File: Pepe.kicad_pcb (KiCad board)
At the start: 2 copper layers, 10 parts, among them P1 USB_OTG, P2 VOC_CONN, P3 DBG_SETPOINT, P4 DBG_VOC, P5 DBG_OUTPUT, U1 ADCMP371, U2 APT7335A-50

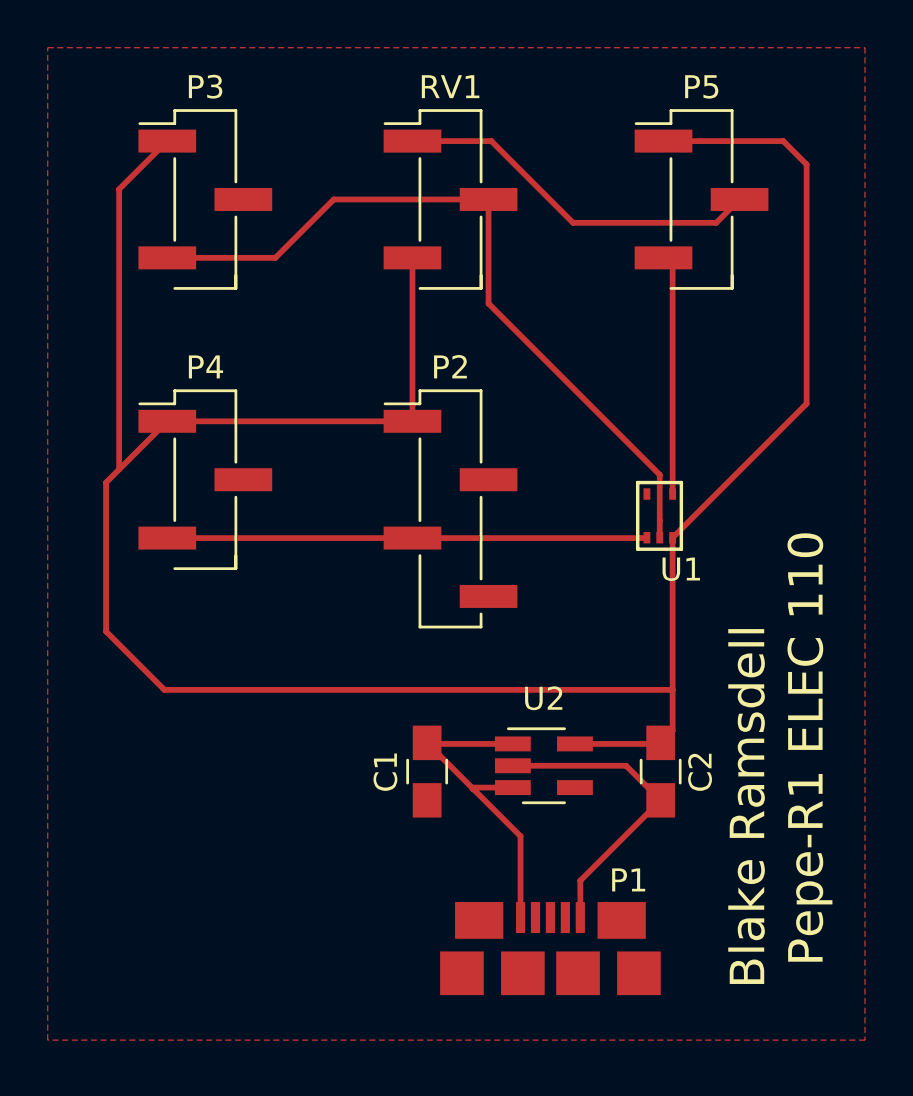
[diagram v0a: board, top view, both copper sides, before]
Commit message: Redid PCB with new comparator. Needs more ground plane work.
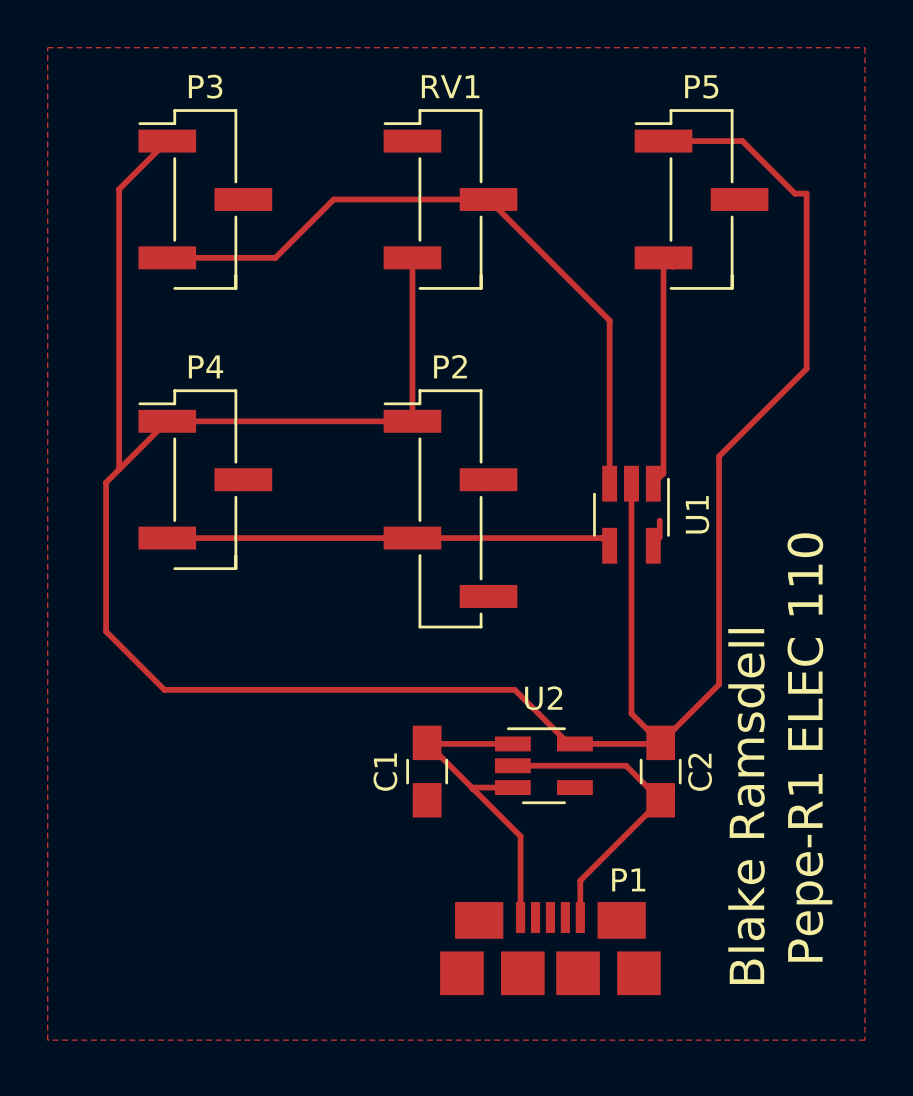
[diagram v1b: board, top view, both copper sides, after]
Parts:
- U1: value ADCMP371 -> MIC7211YM5; footprint Pepe:SC70 -> TO_SOT_Packages_SMD:SOT-23-5_HandSoldering
- moved U1 1.27 mm to (91.4, 61.0), turned to 270 degrees
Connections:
- U1 pad 1: VOC -> OUTPUT
- U1 pad 2: SETPOINT -> +5V
- U1 pad 3: +5V -> SETPOINT
- U1 pad 4: GND -> VOC
- U1 pad 5: OUTPUT -> GND
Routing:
- net GND: track 29.7 -> 14.3 mm
- net +5V: track 107.1 -> 115.6 mm
- net SETPOINT: track 32.8 -> 29.6 mm
- net VOC: track 20.9 -> 19.4 mm
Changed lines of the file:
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@@
     (thickness 1.6)
     (drawings 2)
-    (tracks 46)
+    (tracks 47)
     (zones 0)
     (modules 10)
@@
     (add_net ~ENABLE)
   )
+  (module TO_SOT_Packages_SMD:SOT-23-5_HandSoldering (layer F.Cu)
+    (at 91.44 60.96 270)
+    (descr "5-pin SOT23 package")
+    (tags "SOT-23-5 hand-soldering")
+    (attr smd)
+    (fp_text reference U1 (at 0 -2.9 270) (layer F.SilkS)
+      (effects (font (size 1 1) (thickness 0.15)))
+    )
+    (fp_text value MIC7211YM5 (at 0 2.9 270) (layer F.Fab) hide
+      (effects (font (size 1 1) (thickness 0.15)))
+    )
+    (fp_text user %R (at 0 0) (layer F.Fab)
+      (effects (font (size 0.5 0.5) (thickness 0.075)))
+    )
+    (fp_line (start -0.9 1.61) (end 0.9 1.61) (layer F.SilkS) (width 0.12))
+    (fp_line (start 0.9 -1.61) (end -1.55 -1.61) (layer F.SilkS) (width 0.12))
+    (fp_line (start -0.9 -0.9) (end -0.25 -1.55) (layer F.Fab) (width 0.1))
+    (fp_line (start 0.9 -1.55) (end -0.25 -1.55) (layer F.Fab) (width 0.1))
+    (fp_line (start -0.9 -0.9) (end -0.9 1.55) (layer F.Fab) (width 0.1))
+    (fp_line (start 0.9 1.55) (end -0.9 1.55) (layer F.Fab) (width 0.1))
+    (fp_line (start 0.9 -1.55) (end 0.9 1.55) (layer F.Fab) (width 0.1))
+    (fp_line (start -2.38 -1.8) (end 2.38 -1.8) (layer F.CrtYd) (width 0.05))
+    (fp_line (start -2.38 -1.8) (end -2.38 1.8) (layer F.CrtYd) (width 0.05))
+    (fp_line (start 2.38 1.8) (end 2.38 -1.8) (layer F.CrtYd) (width 0.05))
+    (fp_line (start 2.38 1.8) (end -2.38 1.8) (layer F.CrtYd) (width 0.05))
+    (pad 1 smd rect (at -1.35 -0.95 270) (size 1.56 0.65) (layers F.Cu F.Paste F.Mask)
+      (net 11 OUTPUT))
+    (pad 2 smd rect (at -1.35 0 270) (size 1.56 0.65) (layers F.Cu F.Paste F.Mask)
+      (net 3 +5V))
+    (pad 3 smd rect (at -1.35 0.95 270) (size 1.56 0.65) (layers F.Cu F.Paste F.Mask)
+      (net 10 SETPOINT))
+    (pad 4 smd rect (at 1.35 0.95 270) (size 1.56 0.65) (layers F.Cu F.Paste F.Mask)
+      (net 9 VOC))
+    (pad 5 smd rect (at 1.35 -0.95 270) (size 1.56 0.65) (layers F.Cu F.Paste F.Mask)
+      (net 1 GND))
+    (model ${KISYS3DMOD}/TO_SOT_Packages_SMD.3dshapes\SOT-23-5.wrl
+      (at (xyz 0 0 0))
+      (scale (xyz 1 1 1))
+      (rotate (xyz 0 0 0))
+    )
+  )
   (module Capacitors_SMD:C_0805_HandSoldering (layer F.Cu)
     (at 82.55 72.136 270)
@@
     )
   )
-  (module Pepe:SC70 (layer F.Cu)
-    (at 92.71 60.96)
-    (fp_text reference U1 (at 0.9 2.4) (layer F.SilkS)
-      (effects (font (size 1 1) (thickness 0.15)))
-    )
-    (fp_text value ADCMP371 (at 0.7 -2.2) (layer F.Fab) hide
-      (effects (font (size 1 1) (thickness 0.15)))
-    )
-    (fp_line (start -1 1.5) (end -1 -1.4) (layer F.SilkS) (width 0.15))
-    (fp_line (start 0.9 1.5) (end -1 1.5) (layer F.SilkS) (width 0.15))
-    (fp_line (start 0.9 -1.4) (end 0.9 1.5) (layer F.SilkS) (width 0.15))
-    (fp_line (start -1 -1.4) (end 0.9 -1.4) (layer F.SilkS) (width 0.15))
-    (pad 5 smd rect (at 0.52 -0.9) (size 0.3 0.5) (layers F.Cu F.Paste F.Mask)
-      (net 11 OUTPUT))
-    (pad 4 smd rect (at -0.6 -0.9) (size 0.3 0.5) (layers F.Cu F.Paste F.Mask)
-      (net 1 GND))
-    (pad 3 smd rect (at 0.52 1) (size 0.3 0.5) (layers F.Cu F.Paste F.Mask)
-      (net 3 +5V))
-    (pad 2 smd rect (at -0.04 1) (size 0.3 0.5) (layers F.Cu F.Paste F.Mask)
-      (net 10 SETPOINT))
-    (pad 1 smd rect (at -0.6 1) (size 0.3 0.5) (layers F.Cu F.Paste F.Mask)
-      (net 9 VOC))
-  )
   (module TO_SOT_Packages_SMD:SOT-23-5_HandSoldering (layer F.Cu)
     (at 87.63 71.882)
@@
     (effects (font (size 1.5 1.5) (thickness 0.3)))
   )
-  (segment (start 81.911 44.704) (end 85.344 44.704) (width 0.25) (layer F.Cu) (net 1) (status 400000))
-  (segment (start 95.127 48.26) (end 96.143 47.244) (width 0.25) (layer F.Cu) (net 1) (status 800000))
-  (segment (start 88.9 48.26) (end 95.127 48.26) (width 0.25) (layer F.Cu) (net 1))
-  (segment (start 85.344 44.704) (end 88.9 48.26) (width 0.25) (layer F.Cu) (net 1))
   (segment (start 86.28 71.882) (end 91.206 71.882) (width 0.25) (layer F.Cu) (net 1) (status 400000))
   (segment (start 91.206 71.882) (end 92.71 73.386) (width 0.25) (layer F.Cu) (net 1) (status 800000))
@@
   (segment (start 84.582 72.918) (end 86.614 74.95) (width 0.25) (layer F.Cu) (net 2))
   (segment (start 86.614 74.95) (end 86.614 78.486) (width 0.25) (layer F.Cu) (net 2) (status 800000))
+  (segment (start 99.06 46.99) (end 99.06 54.61) (width 0.25) (layer F.Cu) (net 3))
+  (segment (start 96.266 44.704) (end 98.552 46.99) (width 0.25) (layer F.Cu) (net 3))
+  (segment (start 98.552 46.99) (end 99.06 46.99) (width 0.25) (layer F.Cu) (net 3))
+  (segment (start 92.833 44.704) (end 96.266 44.704) (width 0.25) (layer F.Cu) (net 3) (status 400000))
+  (segment (start 95.25 68.346) (end 92.71 70.886) (width 0.25) (layer F.Cu) (net 3) (status 800000))
+  (segment (start 95.25 58.42) (end 95.25 68.346) (width 0.25) (layer F.Cu) (net 3))
+  (segment (start 99.06 54.61) (end 95.25 58.42) (width 0.25) (layer F.Cu) (net 3))
+  (segment (start 91.44 59.61) (end 91.44 69.616) (width 0.25) (layer F.Cu) (net 3) (status 400000))
+  (segment (start 91.44 69.616) (end 92.71 70.886) (width 0.25) (layer F.Cu) (net 3) (status 800000))
+  (segment (start 88.98 70.932) (end 88.712 70.932) (width 0.25) (layer F.Cu) (net 3) (status C00000))
+  (segment (start 88.712 70.932) (end 86.36 68.58) (width 0.25) (layer F.Cu) (net 3) (status 400000))
   (segment (start 69.1495 58.9895) (end 69.1495 46.7975) (width 0.25) (layer F.Cu) (net 3))
   (segment (start 69.1495 46.7975) (end 71.243 44.704) (width 0.25) (layer F.Cu) (net 3) (status 800000))
   (segment (start 71.243 56.896) (end 81.911 56.896) (width 0.25) (layer F.Cu) (net 3) (status C00000))
-  (segment (start 93.23 68.58) (end 71.12 68.58) (width 0.25) (layer F.Cu) (net 3))
+  (segment (start 86.36 68.58) (end 71.12 68.58) (width 0.25) (layer F.Cu) (net 3))
   (segment (start 68.58 59.559) (end 69.1495 58.9895) (width 0.25) (layer F.Cu) (net 3))
   (segment (start 69.1495 58.9895) (end 71.243 56.896) (width 0.25) (layer F.Cu) (net 3) (status 800000))
   (segment (start 68.58 66.04) (end 68.58 59.559) (width 0.25) (layer F.Cu) (net 3))
   (segment (start 71.12 68.58) (end 68.58 66.04) (width 0.25) (layer F.Cu) (net 3))
-  (segment (start 92.833 44.704) (end 98.044 44.704) (width 0.25) (layer F.Cu) (net 3) (status 400000))
-  (segment (start 99.06 56.13) (end 93.23 61.96) (width 0.25) (layer F.Cu) (net 3) (status 800000))
-  (segment (start 99.06 45.72) (end 99.06 56.13) (width 0.25) (layer F.Cu) (net 3))
-  (segment (start 98.044 44.704) (end 99.06 45.72) (width 0.25) (layer F.Cu) (net 3))
   (segment (start 81.911 49.784) (end 81.911 56.896) (width 0.25) (layer F.Cu) (net 3) (status C00000))
-  (segment (start 93.23 61.96) (end 93.23 68.58) (width 0.25) (layer F.Cu) (net 3) (status 400000))
-  (segment (start 93.23 68.58) (end 93.23 70.366) (width 0.25) (layer F.Cu) (net 3) (status 800000))
   (segment (start 93.23 70.366) (end 92.71 70.886) (width 0.25) (layer F.Cu) (net 3) (status C00000))
   (segment (start 88.98 70.932) (end 92.664 70.932) (width 0.25) (layer F.Cu) (net 3) (status C00000))
   (segment (start 92.664 70.932) (end 92.71 70.886) (width 0.25) (layer F.Cu) (net 3) (status C00000))
+  (segment (start 81.911 61.976) (end 90.156 61.976) (width 0.25) (layer F.Cu) (net 9) (status 400000))
+  (segment (start 90.156 61.976) (end 90.49 62.31) (width 0.25) (layer F.Cu) (net 9) (status 800000))
   (segment (start 71.243 61.976) (end 81.911 61.976) (width 0.25) (layer F.Cu) (net 9) (status C00000))
-  (segment (start 81.911 61.976) (end 92.094 61.976) (width 0.25) (layer F.Cu) (net 9) (status C00000))
-  (segment (start 92.094 61.976) (end 92.11 61.96) (width 0.25) (layer F.Cu) (net 9) (status C00000))
+  (segment (start 90.49 59.61) (end 90.49 52.513) (width 0.25) (layer F.Cu) (net 10) (status 400000))
+  (segment (start 90.49 52.513) (end 85.221 47.244) (width 0.25) (layer F.Cu) (net 10) (status 800000))
   (segment (start 71.243 49.784) (end 75.946 49.784) (width 0.25) (layer F.Cu) (net 10) (status 400000))
   (segment (start 78.486 47.244) (end 85.221 47.244) (width 0.25) (layer F.Cu) (net 10) (status 800000))
   (segment (start 75.946 49.784) (end 78.486 47.244) (width 0.25) (layer F.Cu) (net 10))
-  (segment (start 92.67 61.96) (end 92.67 61.214) (width 0.25) (layer F.Cu) (net 10) (status 400000))
-  (segment (start 92.67 61.214) (end 92.67 59.222) (width 0.25) (layer F.Cu) (net 10))
-  (segment (start 85.221 51.773) (end 85.221 47.244) (width 0.25) (layer F.Cu) (net 10) (status 800000))
-  (segment (start 92.67 59.222) (end 85.221 51.773) (width 0.25) (layer F.Cu) (net 10))
-  (segment (start 93.23 60.06) (end 93.23 50.181) (width 0.25) (layer F.Cu) (net 11) (status C00000))
+  (segment (start 92.67 61.96) (end 92.67 61.214) (width 0.25) (layer F.Cu) (net 1) (status 400000))
+  (segment (start 92.833 49.784) (end 92.833 59.167) (width 0.25) (layer F.Cu) (net 11) (status 400000))
+  (segment (start 92.833 59.167) (end 92.39 59.61) (width 0.25) (layer F.Cu) (net 11) (status 800000))
   (segment (start 93.23 50.181) (end 92.833 49.784) (width 0.25) (layer F.Cu) (net 11) (status C00000))
   (zone (net 1) (net_name GND) (layer F.Cu) (hatch edge 0.508)

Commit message: R1 PCB might be done. No ERC or DRC errors.
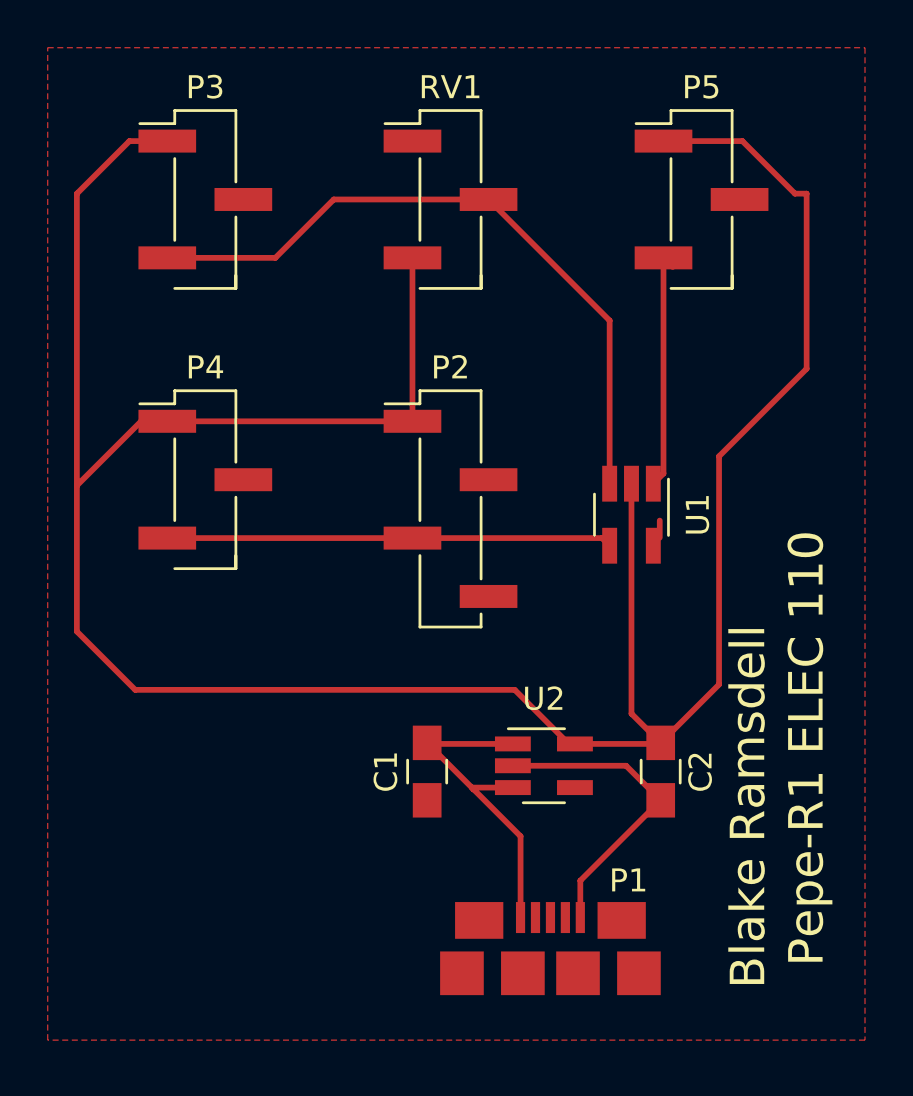
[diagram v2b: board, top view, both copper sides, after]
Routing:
- net +5V: track 115.6 -> 120.5 mm
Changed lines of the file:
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@@
     (thickness 1.6)
     (drawings 2)
-    (tracks 47)
+    (tracks 48)
     (zones 0)
     (modules 10)
@@
   (segment (start 84.582 72.918) (end 86.614 74.95) (width 0.25) (layer F.Cu) (net 2))
   (segment (start 86.614 74.95) (end 86.614 78.486) (width 0.25) (layer F.Cu) (net 2) (status 800000))
+  (segment (start 67.31 59.69) (end 67.31 46.99) (width 0.25) (layer F.Cu) (net 3))
+  (segment (start 69.596 44.704) (end 71.243 44.704) (width 0.25) (layer F.Cu) (net 3) (status 800000))
+  (segment (start 67.31 46.99) (end 69.596 44.704) (width 0.25) (layer F.Cu) (net 3))
+  (segment (start 67.31 66.04) (end 67.31 59.69) (width 0.25) (layer F.Cu) (net 3))
+  (segment (start 86.36 68.58) (end 69.85 68.58) (width 0.25) (layer F.Cu) (net 3))
+  (segment (start 69.85 68.58) (end 67.31 66.04) (width 0.25) (layer F.Cu) (net 3))
+  (segment (start 88.712 70.932) (end 86.36 68.58) (width 0.25) (layer F.Cu) (net 3) (status 400000))
+  (segment (start 67.31 59.69) (end 70.104 56.896) (width 0.25) (layer F.Cu) (net 3) (status 800000))
+  (segment (start 70.104 56.896) (end 71.243 56.896) (width 0.25) (layer F.Cu) (net 3) (status C00000))
+  (segment (start 88.98 70.932) (end 88.712 70.932) (width 0.25) (layer F.Cu) (net 3) (status C00000))
   (segment (start 99.06 46.99) (end 99.06 54.61) (width 0.25) (layer F.Cu) (net 3))
   (segment (start 96.266 44.704) (end 98.552 46.99) (width 0.25) (layer F.Cu) (net 3))
@@
   (segment (start 91.44 59.61) (end 91.44 69.616) (width 0.25) (layer F.Cu) (net 3) (status 400000))
   (segment (start 91.44 69.616) (end 92.71 70.886) (width 0.25) (layer F.Cu) (net 3) (status 800000))
-  (segment (start 88.98 70.932) (end 88.712 70.932) (width 0.25) (layer F.Cu) (net 3) (status C00000))
-  (segment (start 88.712 70.932) (end 86.36 68.58) (width 0.25) (layer F.Cu) (net 3) (status 400000))
-  (segment (start 69.1495 58.9895) (end 69.1495 46.7975) (width 0.25) (layer F.Cu) (net 3))
-  (segment (start 69.1495 46.7975) (end 71.243 44.704) (width 0.25) (layer F.Cu) (net 3) (status 800000))
   (segment (start 71.243 56.896) (end 81.911 56.896) (width 0.25) (layer F.Cu) (net 3) (status C00000))
-  (segment (start 86.36 68.58) (end 71.12 68.58) (width 0.25) (layer F.Cu) (net 3))
-  (segment (start 68.58 59.559) (end 69.1495 58.9895) (width 0.25) (layer F.Cu) (net 3))
-  (segment (start 69.1495 58.9895) (end 71.243 56.896) (width 0.25) (layer F.Cu) (net 3) (status 800000))
-  (segment (start 68.58 66.04) (end 68.58 59.559) (width 0.25) (layer F.Cu) (net 3))
-  (segment (start 71.12 68.58) (end 68.58 66.04) (width 0.25) (layer F.Cu) (net 3))
   (segment (start 81.911 49.784) (end 81.911 56.896) (width 0.25) (layer F.Cu) (net 3) (status C00000))
   (segment (start 93.23 70.366) (end 92.71 70.886) (width 0.25) (layer F.Cu) (net 3) (status C00000))

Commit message: Edge cuts for board outline.
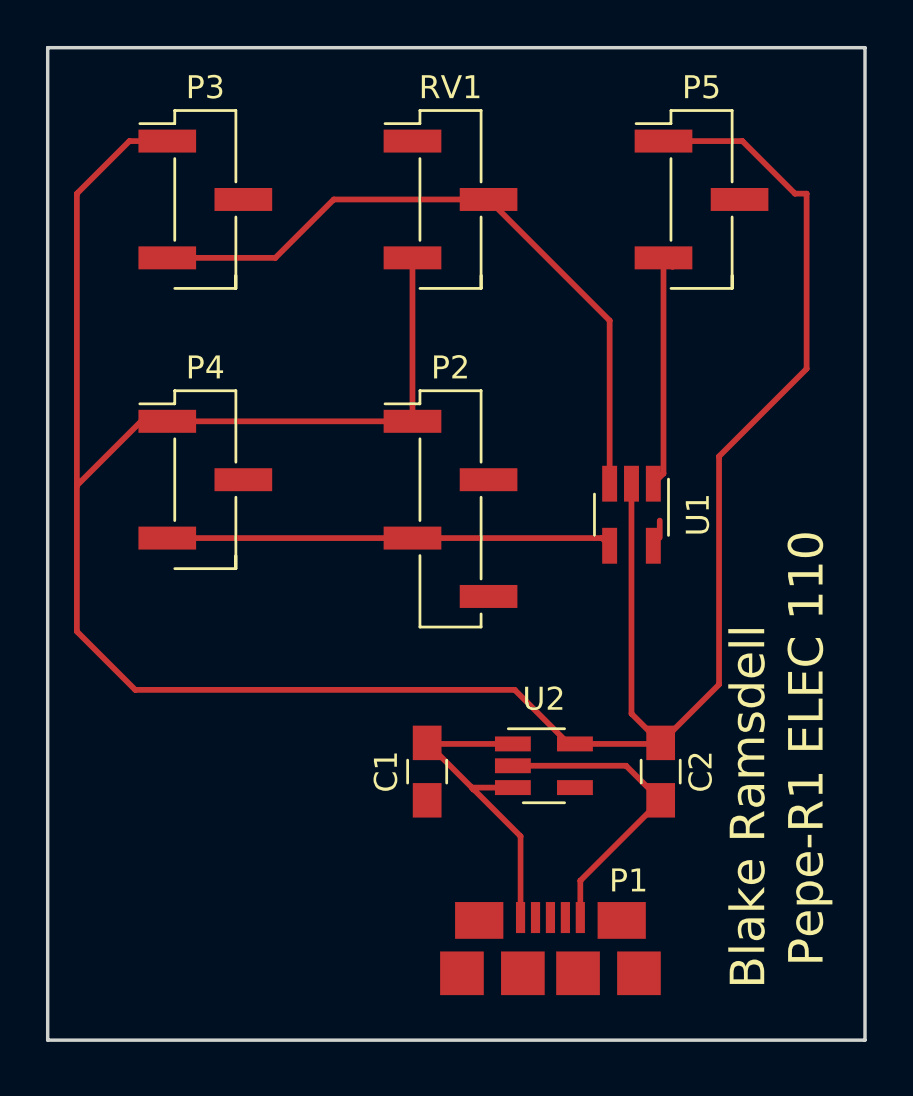
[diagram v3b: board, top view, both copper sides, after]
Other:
- board outline added: 35.6 x 43.2 mm
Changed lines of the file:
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@@
   (general
     (thickness 1.6)
-    (drawings 2)
+    (drawings 6)
     (tracks 48)
     (zones 0)
@@
     )
   )
+  (gr_line (start 66.04 83.82) (end 66.04 40.64) (angle 90) (layer Edge.Cuts) (width 0.15))
+  (gr_line (start 101.6 83.82) (end 66.04 83.82) (angle 90) (layer Edge.Cuts) (width 0.15))
+  (gr_line (start 101.6 40.64) (end 101.6 83.82) (angle 90) (layer Edge.Cuts) (width 0.15))
+  (gr_line (start 66.04 40.64) (end 101.6 40.64) (angle 90) (layer Edge.Cuts) (width 0.15))
   (gr_text "Pepe-R1 ELEC 110" (at 99.06 71.12 90) (layer F.SilkS)
     (effects (font (size 1.5 1.5) (thickness 0.3)))
